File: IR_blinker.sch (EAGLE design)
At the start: 11 parts, among them IC1 PIC16F15214-E/SN, Q1 DMG2302UK

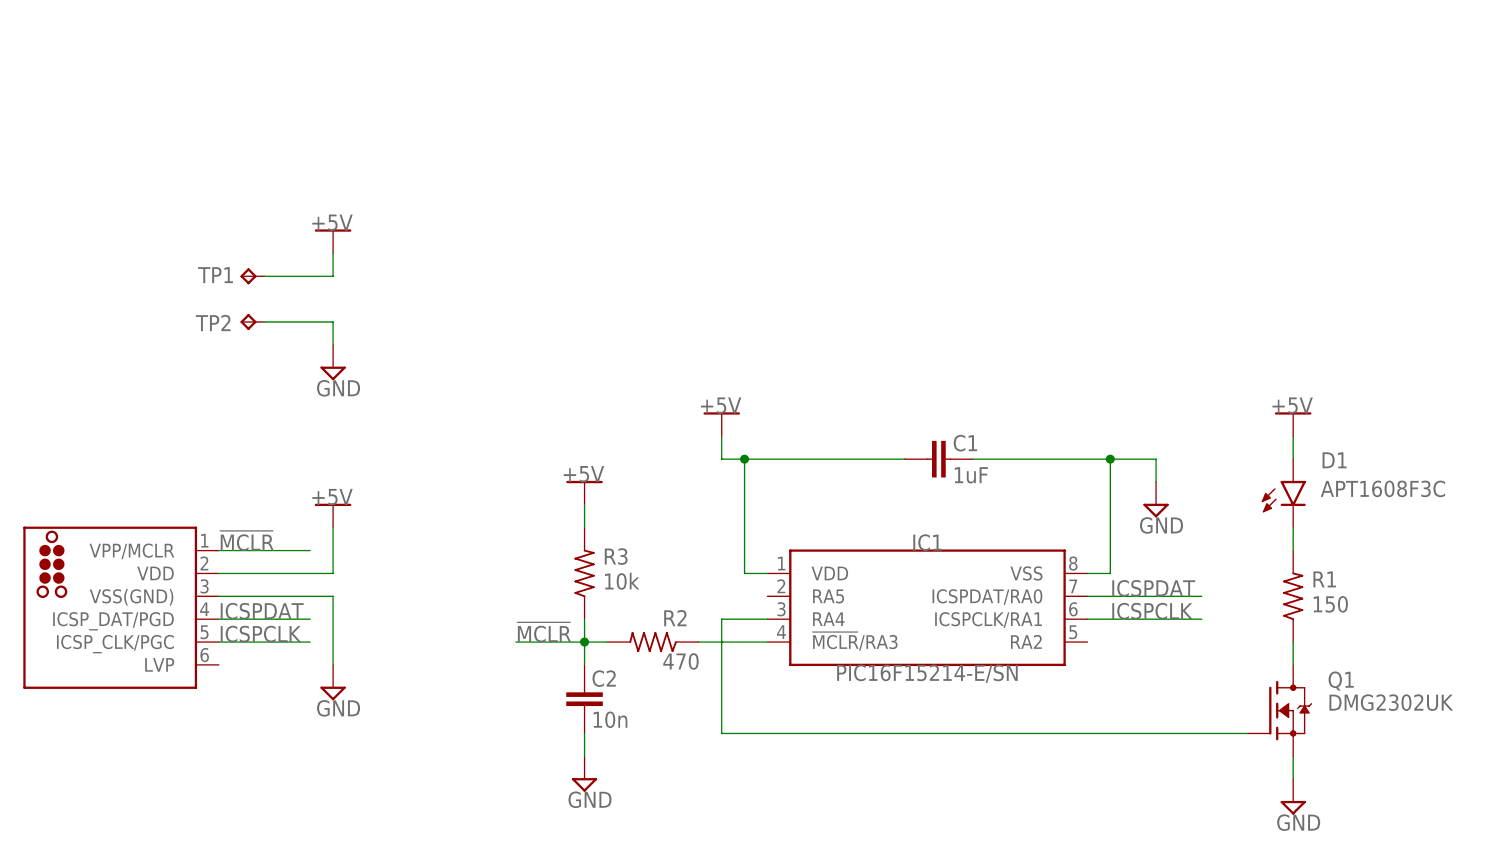
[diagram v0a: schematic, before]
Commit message: Linear Regulator added. Passives added to MCLR.
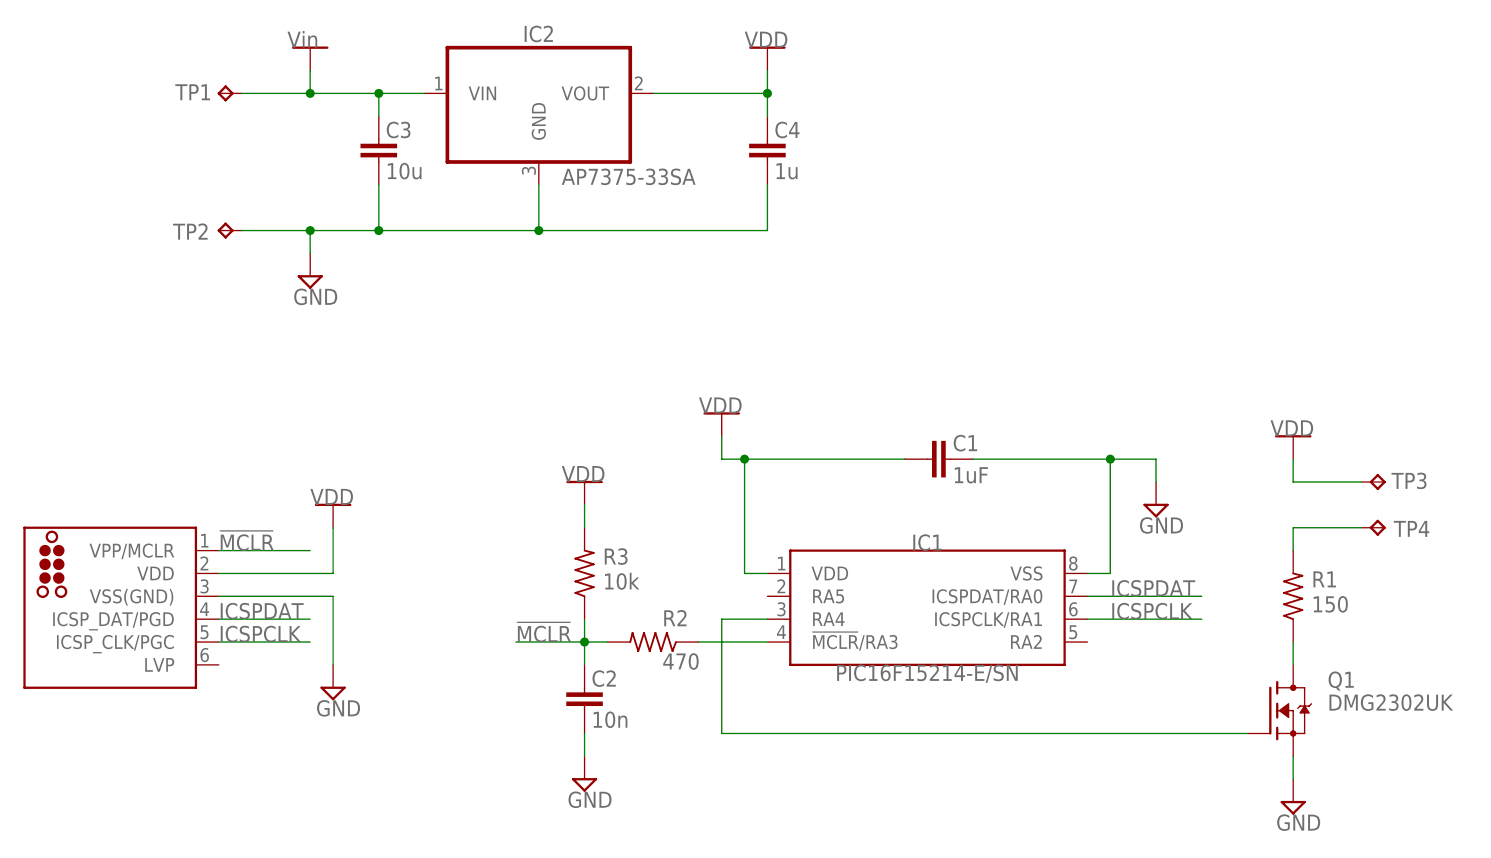
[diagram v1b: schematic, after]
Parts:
- removed D1: APT1608F3C, led:LEDCHIP-LED0603
- added C3: 10u, rcl:C-EUC0603
- added C4: 1u, rcl:C-EUC0603
- added IC2: AP7375-33SA, Diodes_Inc:AP7375-33SA
- added TP3, TP4: TPTP20SQ, testpad:TPTP20SQ
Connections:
- removed net +5V: C1.1, D1.A, IC1.VDD, J1.VDD, R3.2, TP1.TP
- removed net N$2: D1.C, R1.2
- new net LED_RETURN: R1.2, TP4.TP
- new net VDD: C1.1, C4.2, IC1.VDD, IC2.VOUT, J1.VDD, R3.2, TP3.TP
- new net VIN: C3.2, IC2.VIN, TP1.TP
- net GND: now also C3.1, C4.1, IC2.GND
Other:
- moved on the sheet: TP1, TP2
